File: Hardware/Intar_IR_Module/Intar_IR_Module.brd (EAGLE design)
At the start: 17.8 x 25.9 mm, 19 parts, among them J2 GROVE-4P-2.0-3470130P1, Q1 MMBT2222A, Q2 MMBT2222A

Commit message: Imported logo into Eagle
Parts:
- added U$1: LOGOSM, Intar_Eagle_Library:LOGO_SM
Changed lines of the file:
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@@
 <layers>
 <layer number="1" name="Top" color="4" fill="1" visible="yes" active="yes"/>
-<layer number="2" name="Route2" color="1" fill="3" visible="yes" active="yes"/>
-<layer number="15" name="Route15" color="4" fill="6" visible="yes" active="yes"/>
+<layer number="2" name="Route2" color="1" fill="3" visible="no" active="yes"/>
+<layer number="15" name="Route15" color="4" fill="6" visible="no" active="yes"/>
 <layer number="16" name="Bottom" color="1" fill="1" visible="yes" active="yes"/>
 <layer number="17" name="Pads" color="2" fill="1" visible="yes" active="yes"/>
@@
 <layer number="23" name="tOrigins" color="15" fill="1" visible="yes" active="yes"/>
 <layer number="24" name="bOrigins" color="15" fill="1" visible="yes" active="yes"/>
-<layer number="25" name="tNames" color="7" fill="1" visible="yes" active="yes"/>
-<layer number="26" name="bNames" color="7" fill="1" visible="yes" active="yes"/>
-<layer number="27" name="tValues" color="7" fill="1" visible="yes" active="yes"/>
-<layer number="28" name="bValues" color="7" fill="1" visible="yes" active="yes"/>
-<layer number="29" name="tStop" color="7" fill="3" visible="yes" active="yes"/>
-<layer number="30" name="bStop" color="7" fill="6" visible="yes" active="yes"/>
-<layer number="31" name="tCream" color="7" fill="4" visible="yes" active="yes"/>
-<layer number="32" name="bCream" color="7" fill="5" visible="yes" active="yes"/>
-<layer number="39" name="tKeepout" color="4" fill="11" visible="yes" active="yes"/>
-<layer number="40" name="bKeepout" color="1" fill="11" visible="yes" active="yes"/>
-<layer number="41" name="tRestrict" color="4" fill="10" visible="yes" active="yes"/>
-<layer number="42" name="bRestrict" color="1" fill="10" visible="yes" active="yes"/>
-<layer number="43" name="vRestrict" color="2" fill="10" visible="yes" active="yes"/>
-<layer number="44" name="Drills" color="7" fill="1" visible="yes" active="yes"/>
+<layer number="25" name="tNames" color="7" fill="1" visible="no" active="yes"/>
+<layer number="26" name="bNames" color="7" fill="1" visible="no" active="yes"/>
+<layer number="27" name="tValues" color="7" fill="1" visible="no" active="yes"/>
+<layer number="28" name="bValues" color="7" fill="1" visible="no" active="yes"/>
+<layer number="29" name="tStop" color="7" fill="3" visible="no" active="yes"/>
+<layer number="30" name="bStop" color="7" fill="6" visible="no" active="yes"/>
+<layer number="31" name="tCream" color="7" fill="4" visible="no" active="yes"/>
+<layer number="32" name="bCream" color="7" fill="5" visible="no" active="yes"/>
+<layer number="39" name="tKeepout" color="4" fill="11" visible="no" active="yes"/>
+<layer number="40" name="bKeepout" color="1" fill="11" visible="no" active="yes"/>
+<layer number="41" name="tRestrict" color="4" fill="10" visible="no" active="yes"/>
+<layer number="42" name="bRestrict" color="1" fill="10" visible="no" active="yes"/>
+<layer number="43" name="vRestrict" color="2" fill="10" visible="no" active="yes"/>
+<layer number="44" name="Drills" color="7" fill="1" visible="no" active="yes"/>
 <layer number="45" name="Holes" color="7" fill="1" visible="yes" active="yes"/>
-<layer number="46" name="Milling" color="3" fill="1" visible="yes" active="yes"/>
-<layer number="47" name="Measures" color="7" fill="1" visible="yes" active="yes"/>
+<layer number="46" name="Milling" color="3" fill="1" visible="no" active="yes"/>
+<layer number="47" name="Measures" color="7" fill="1" visible="no" active="yes"/>
 <layer number="51" name="tDocu" color="6" fill="1" visible="yes" active="yes"/>
-<layer number="52" name="bDocu" color="7" fill="1" visible="yes" active="yes"/>
+<layer number="52" name="bDocu" color="7" fill="1" visible="no" active="yes"/>
 <layer number="3" name="Route3" color="4" fill="3" visible="no" active="no"/>
 <layer number="4" name="Route4" color="1" fill="4" visible="no" active="no"/>
@@
 <text x="-24.384" y="-8.89" size="0.889" layer="22" font="vector" ratio="15" rot="MR180" align="top-center">IR</text>
 <text x="-22.352" y="-8.89" size="0.889" layer="22" font="vector" ratio="15" rot="MR180" align="top-center">L</text>
-<polygon width="0.0254" layer="22">
-<vertex x="-25.146" y="18.669"/>
-<vertex x="-25.146" y="18.161"/>
-<vertex x="-25.654" y="18.161"/>
-<vertex x="-25.654" y="16.129"/>
-<vertex x="-25.146" y="16.129"/>
-<vertex x="-25.146" y="15.621"/>
-<vertex x="-26.67" y="15.621"/>
-<vertex x="-26.67" y="16.129"/>
-<vertex x="-26.162" y="16.129"/>
-<vertex x="-26.162" y="18.161"/>
-<vertex x="-26.67" y="18.161"/>
-<vertex x="-26.67" y="18.669"/>
-</polygon>
-<polygon width="0.0254" layer="22">
-<vertex x="-26.67" y="18.669"/>
-<vertex x="-26.67" y="15.621"/>
-<vertex x="-27.178" y="15.621"/>
-<vertex x="-27.178" y="16.891"/>
-<vertex x="-27.686" y="16.891"/>
-<vertex x="-27.686" y="15.621"/>
-<vertex x="-28.194" y="15.621"/>
-<vertex x="-28.194" y="18.669"/>
-<vertex x="-27.686" y="18.669"/>
-<vertex x="-27.686" y="17.399"/>
-<vertex x="-27.178" y="17.399"/>
-<vertex x="-27.178" y="18.669"/>
-</polygon>
-<polygon width="0.0254" layer="22">
-<vertex x="-28.194" y="18.669"/>
-<vertex x="-28.194" y="18.161"/>
-<vertex x="-28.702" y="18.161"/>
-<vertex x="-28.702" y="16.129"/>
-<vertex x="-28.194" y="16.129"/>
-<vertex x="-28.194" y="15.621"/>
-<vertex x="-29.718" y="15.621"/>
-<vertex x="-29.718" y="16.129"/>
-<vertex x="-29.21" y="16.129"/>
-<vertex x="-29.21" y="18.161"/>
-<vertex x="-29.718" y="18.161"/>
-<vertex x="-29.718" y="18.669"/>
-</polygon>
 <text x="-44.45" y="1.27" size="1.27" layer="22" font="vector" ratio="15" rot="MR0" align="center">Intar
 IR LED Module</text>
@@
 <element name="STANDOFF2" library="SparkFun-Electromechanical" package="STAND-OFF" value="STAND-OFF" x="0" y="10.16"/>
 <element name="J2" library="Connector" package="4P-2.0" value="GROVE-4P-2.0-3470130P1" x="-48.26" y="-27.94" rot="MR0"/>
+<element name="U$1" library="Intar_Eagle_Library" package="LOGO_SM" value="LOGOSM" x="-41.275" y="-4.318" rot="MR0"/>
 </elements>
 <signals>

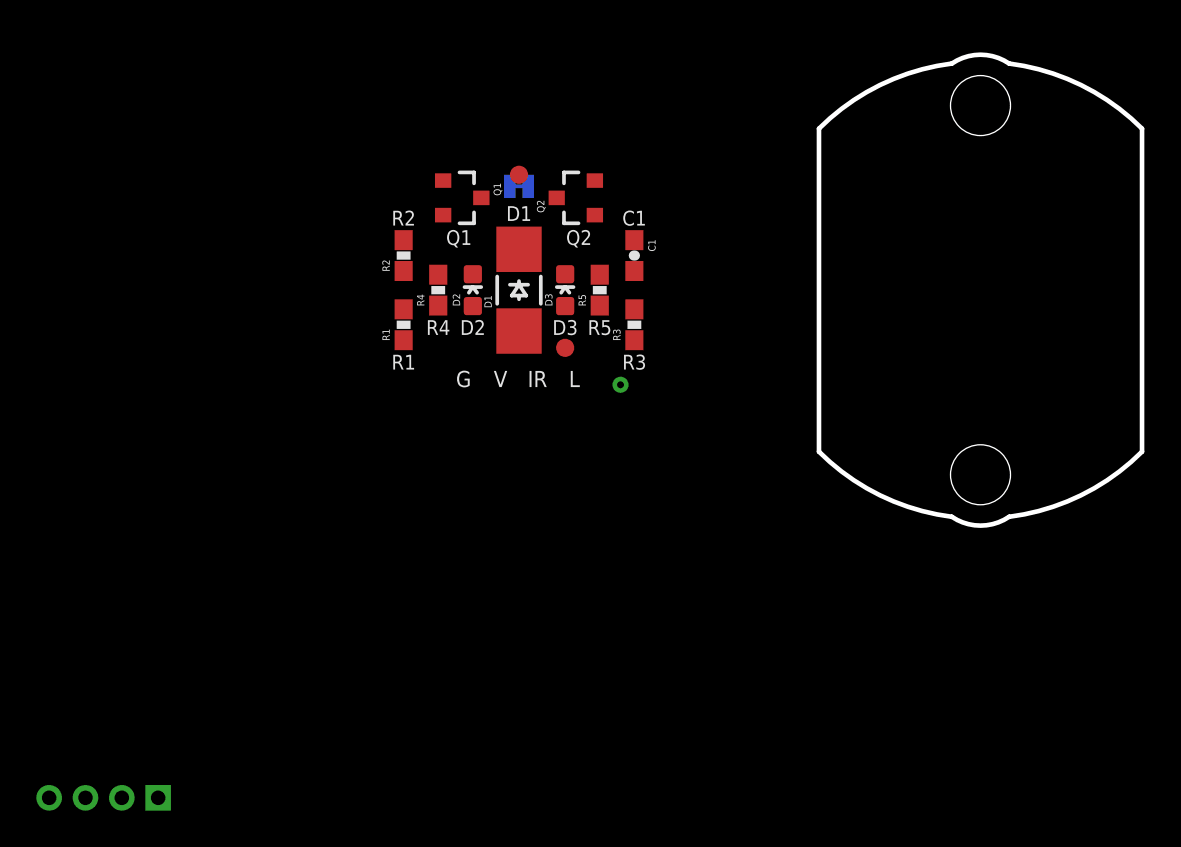
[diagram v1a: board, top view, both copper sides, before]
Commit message: Arranged components on all modules
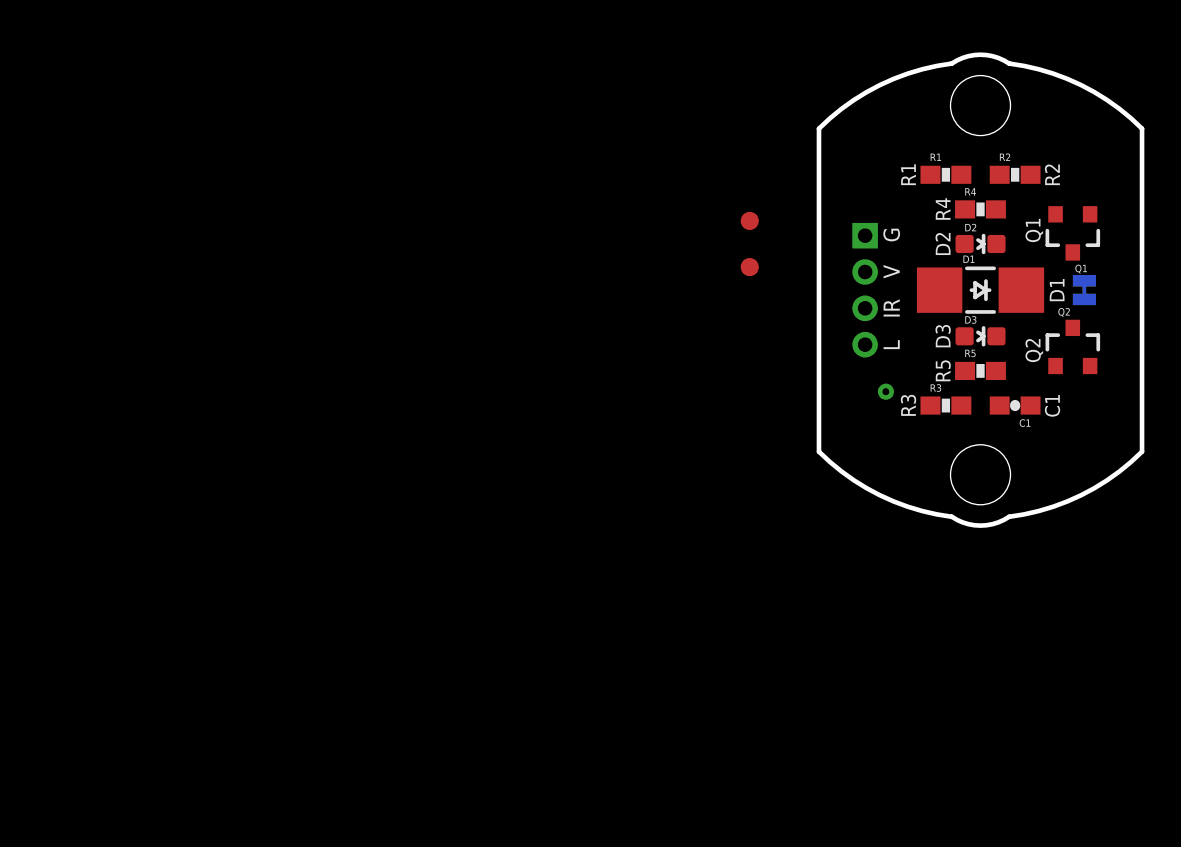
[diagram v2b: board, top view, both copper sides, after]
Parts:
- moved J2 50.4 mm to (-6.35, 0.00), turned to 270 degrees
- moved R2 33.9 mm to (1.91, 6.35), turned to 0 degrees
- moved Q1 33.7 mm to (5.08, 3.17), turned to 180 degrees
- moved SJ1 31.6 mm to (5.71, 0.00), turned to 90 degrees
- moved R1 31.0 mm to (-1.91, 6.35), turned to 0 degrees
- moved R4 30.2 mm to (0.00, 4.45), turned to 0 degrees
- moved Q2 28.5 mm to (5.08, -3.17), turned to 0 degrees
- moved D2 28.1 mm to (0.00, 2.54), turned to 270 degrees
- moved D1 25.4 mm to (0.00, 0.00), turned to 270 degrees
- moved D3 23.0 mm to (0.00, -2.54), turned to 270 degrees
- moved C1 22.5 mm to (1.91, -6.35), turned to 180 degrees
- moved R5 21.4 mm to (0.00, -4.45), turned to 0 degrees
- moved R3 17.7 mm to (-1.91, -6.35), turned to 0 degrees
- moved FID1 13.0 mm to (-12.7, 3.81), turned to 270 degrees
- moved FID2 11.1 mm to (-12.7, 1.27), turned to 270 degrees

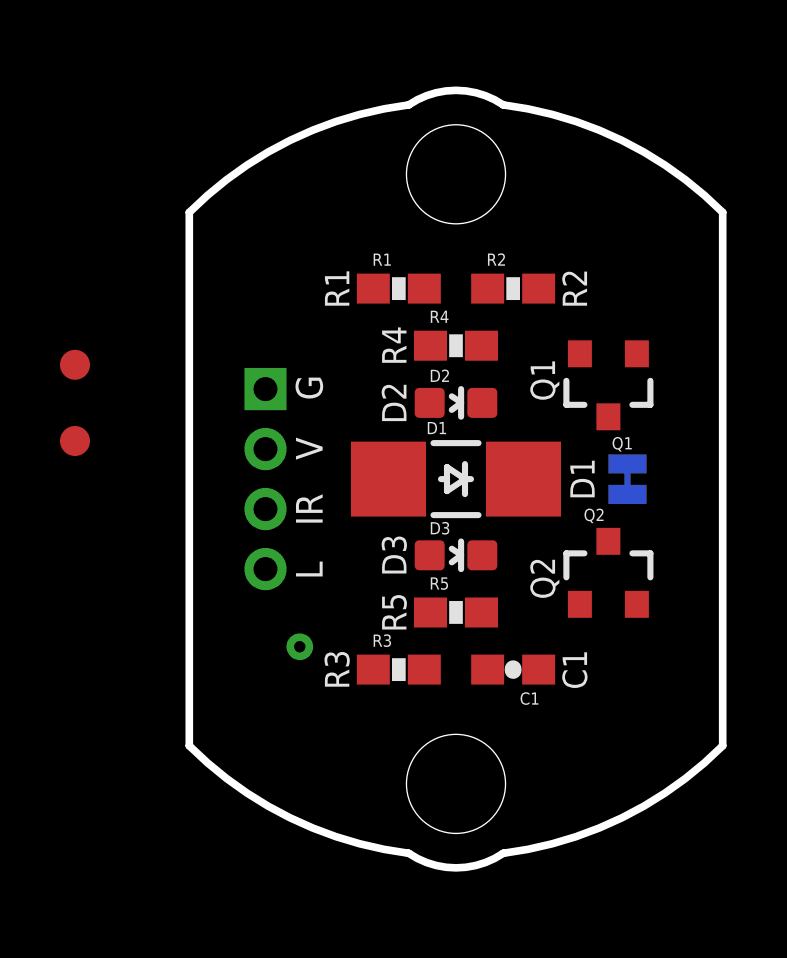
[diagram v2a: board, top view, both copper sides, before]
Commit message: Finished RGB and IR modules
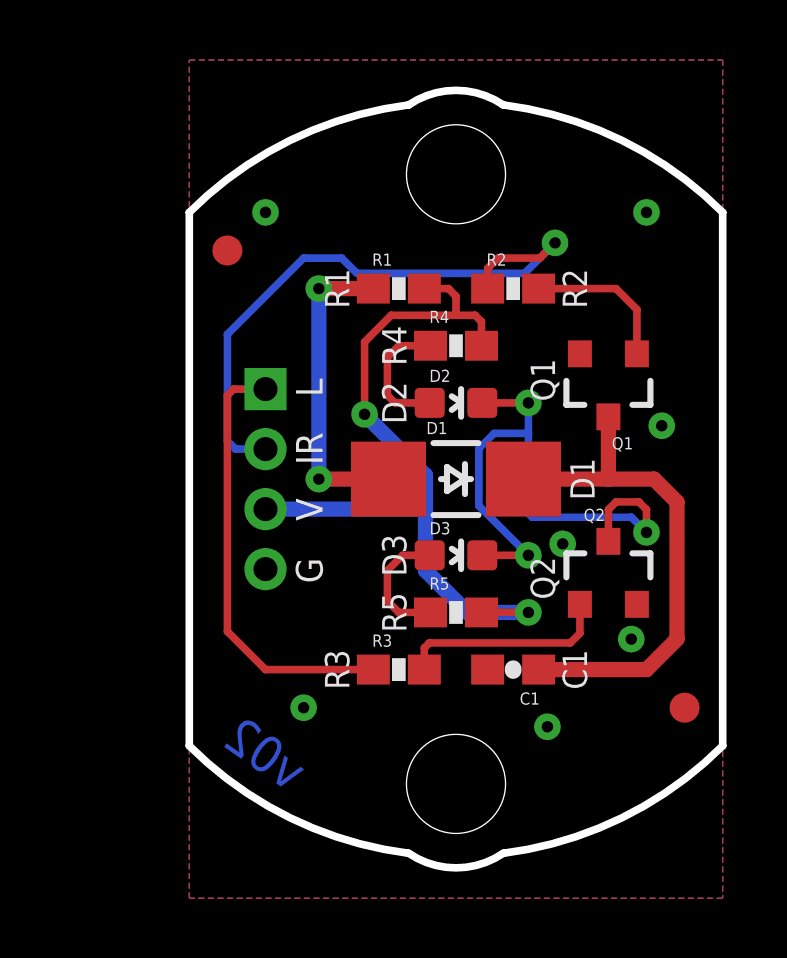
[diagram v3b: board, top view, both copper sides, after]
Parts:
- moved LOGO1 52.9 mm to (5.08, 8.26), turned to 270 degrees
- moved U$1 46.5 mm to (5.08, -8.26), turned to 270 degrees
- moved FID2 22.2 mm to (7.62, -7.62)
- moved FID1 6.35 mm to (-7.62, 7.62)
- moved SJ1 3.30 mm to (2.41, 0.00)
- renumbered J2 to J1
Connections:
- net GND: now also J1.4; no longer J1.1
- net IR: now also J1.2; no longer J1.3
- net LEDS: now also J1.1; no longer J1.4
- net VCC: now also J1.3; no longer J1.2
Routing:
- net VCC: track 0.00 -> 26.3 mm, vias 0 -> 2
- net IR: track 0.00 -> 20.8 mm, vias 0 -> 1
- net N$3: track 0.00 -> 17.1 mm
- net LEDS: track 0.00 -> 14.6 mm
- net N$4: track 0.00 -> 11.2 mm, vias 0 -> 2
- net N$2: track 0.00 -> 10.5 mm, vias 0 -> 2
- net N$8: track 0.00 -> 8.14 mm, vias 0 -> 1
- net N$5: track 0.00 -> 7.08 mm
- net N$1: track 0.00 -> 5.04 mm
- net N$6: track 0.00 -> 4.38 mm
- net N$7: track 0.00 -> 4.23 mm
- added copper zone on layer 1, net GND
- added copper zone on layer 16, net GND
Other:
- board text added: "Intar IR Module"
- board text added: "v02"
- board text removed: "Intar IR LED Module"
- board text removed: "v01"

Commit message: Completed Vibration Module v01 layout
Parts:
- moved LOGO1 0.63 mm to (4.45, 8.26)
- moved U$1 0.63 mm to (4.45, -8.26)
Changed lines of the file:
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@@
 <setting verticaltext="up"/>
 </settings>
-<grid distance="0.01" unitdist="inch" unit="inch" style="dots" multiple="1" display="yes" altdistance="0.005" altunitdist="inch" altunit="inch"/>
+<grid distance="0.05" unitdist="inch" unit="inch" style="dots" multiple="1" display="yes" altdistance="0.005" altunitdist="inch" altunit="inch"/>
 <layers>
-<layer number="1" name="Top" color="4" fill="1" visible="yes" active="yes"/>
+<layer number="1" name="Top" color="4" fill="1" visible="no" active="yes"/>
 <layer number="2" name="Route2" color="1" fill="3" visible="no" active="yes"/>
 <layer number="15" name="Route15" color="4" fill="6" visible="no" active="yes"/>
@@
 <layer number="19" name="Unrouted" color="6" fill="1" visible="yes" active="yes"/>
 <layer number="20" name="Dimension" color="15" fill="1" visible="yes" active="yes"/>
-<layer number="21" name="tPlace" color="16" fill="1" visible="yes" active="yes"/>
+<layer number="21" name="tPlace" color="16" fill="1" visible="no" active="yes"/>
 <layer number="22" name="bPlace" color="14" fill="1" visible="yes" active="yes"/>
-<layer number="23" name="tOrigins" color="15" fill="1" visible="yes" active="yes"/>
+<layer number="23" name="tOrigins" color="15" fill="1" visible="no" active="yes"/>
 <layer number="24" name="bOrigins" color="15" fill="1" visible="yes" active="yes"/>
 <layer number="25" name="tNames" color="7" fill="1" visible="no" active="yes"/>
@@
 <layer number="43" name="vRestrict" color="2" fill="10" visible="no" active="yes"/>
 <layer number="44" name="Drills" color="7" fill="1" visible="no" active="yes"/>
-<layer number="45" name="Holes" color="7" fill="1" visible="yes" active="yes"/>
+<layer number="45" name="Holes" color="7" fill="1" visible="no" active="yes"/>
 <layer number="46" name="Milling" color="3" fill="1" visible="no" active="yes"/>
-<layer number="47" name="Measures" color="7" fill="1" visible="yes" active="yes"/>
-<layer number="51" name="tDocu" color="6" fill="1" visible="yes" active="yes"/>
+<layer number="47" name="Measures" color="7" fill="1" visible="no" active="yes"/>
+<layer number="51" name="tDocu" color="6" fill="1" visible="no" active="yes"/>
 <layer number="52" name="bDocu" color="7" fill="1" visible="no" active="yes"/>
 <layer number="3" name="Route3" color="4" fill="3" visible="no" active="no"/>
@@
 <element name="FID2" library="SparkFun-Aesthetics" package="FIDUCIAL-1X2" value="FIDUCIAL1X2" x="7.62" y="-7.62" rot="R270"/>
 <element name="FRAME1" library="SparkFun-Aesthetics" package="CREATIVE_COMMONS" value="FRAME-LETTER" x="-33.02" y="-22.86"/>
-<element name="LOGO1" library="SparkFun-Aesthetics" package="OSHW-LOGO-S" value="OSHW-LOGOS" x="5.08" y="8.255" rot="MR270"/>
+<element name="LOGO1" library="SparkFun-Aesthetics" package="OSHW-LOGO-S" value="OSHW-LOGOS" x="4.445" y="8.255" rot="MR270"/>
 <element name="Q1" library="SparkFun-DiscreteSemi" package="SOT23-3" value="MMBT2222A" x="5.08" y="3.175" rot="R180">
 <attribute name="PROD_ID" value="TRANS-08049" x="5.08" y="3.175" size="1.778" layer="27" rot="R180" display="off"/>
@@
 <element name="STANDOFF1" library="SparkFun-Electromechanical" package="STAND-OFF" value="STAND-OFF" x="0" y="-10.16"/>
 <element name="STANDOFF2" library="SparkFun-Electromechanical" package="STAND-OFF" value="STAND-OFF" x="0" y="10.16"/>
-<element name="U$1" library="Intar_Eagle_Library" package="LOGO_SM" value="LOGOSM" x="5.08" y="-8.255" rot="MR270"/>
+<element name="U$1" library="Intar_Eagle_Library" package="LOGO_SM" value="LOGOSM" x="4.445" y="-8.255" rot="MR270"/>
 <element name="J1" library="Connector" package="4P-2.0" value="GROVE-4P-2.0-3470130P1" x="-6.35" y="0" rot="MR270"/>
 </elements>
